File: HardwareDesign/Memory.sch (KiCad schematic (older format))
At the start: 4 parts, among them U200 28C256, U201 HM62256BLP-7SL

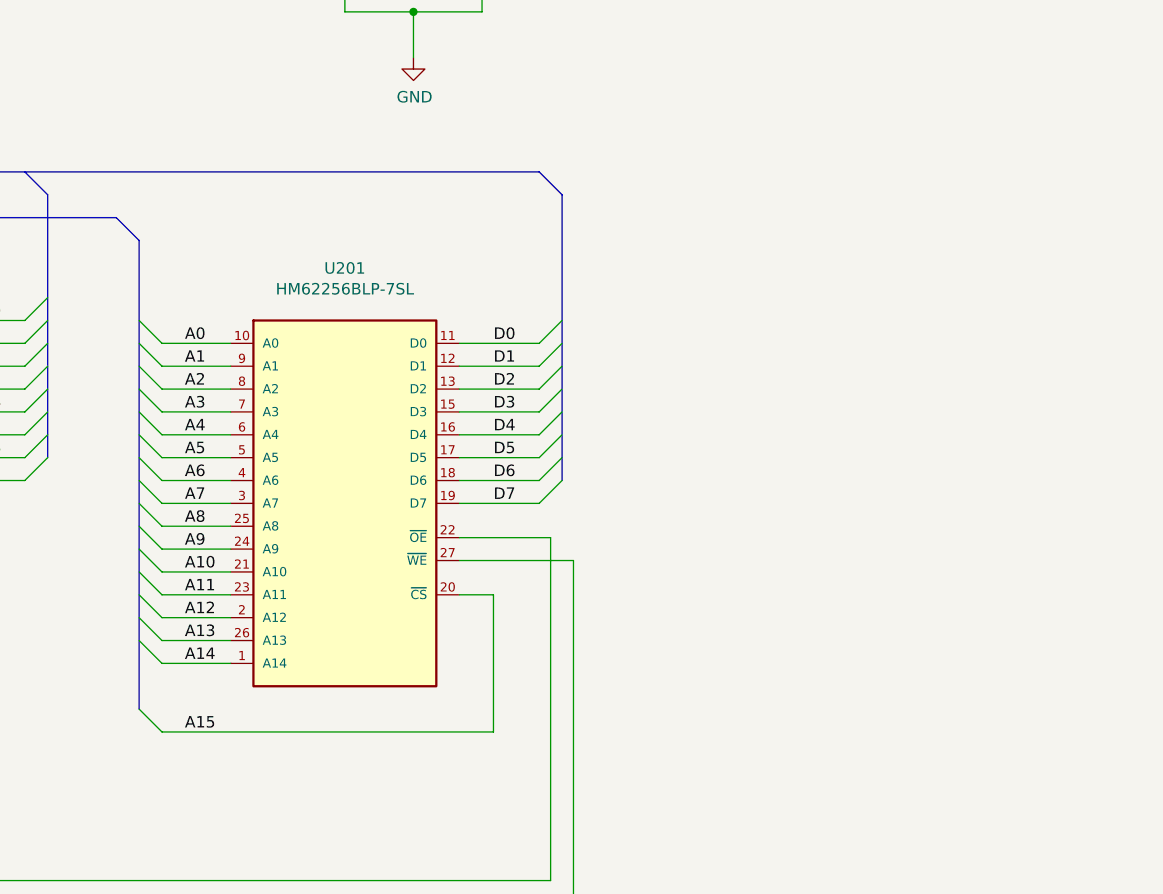
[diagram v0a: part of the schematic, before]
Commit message: added ~RAMEN~ backplane signals
Added a jumper so that the RAM chip can be configured
to use either A15 or ~RAMEN~ as its enable.

This change allows a CPU/glue logic module to have flexibility
regarding where the RAM is mapped.
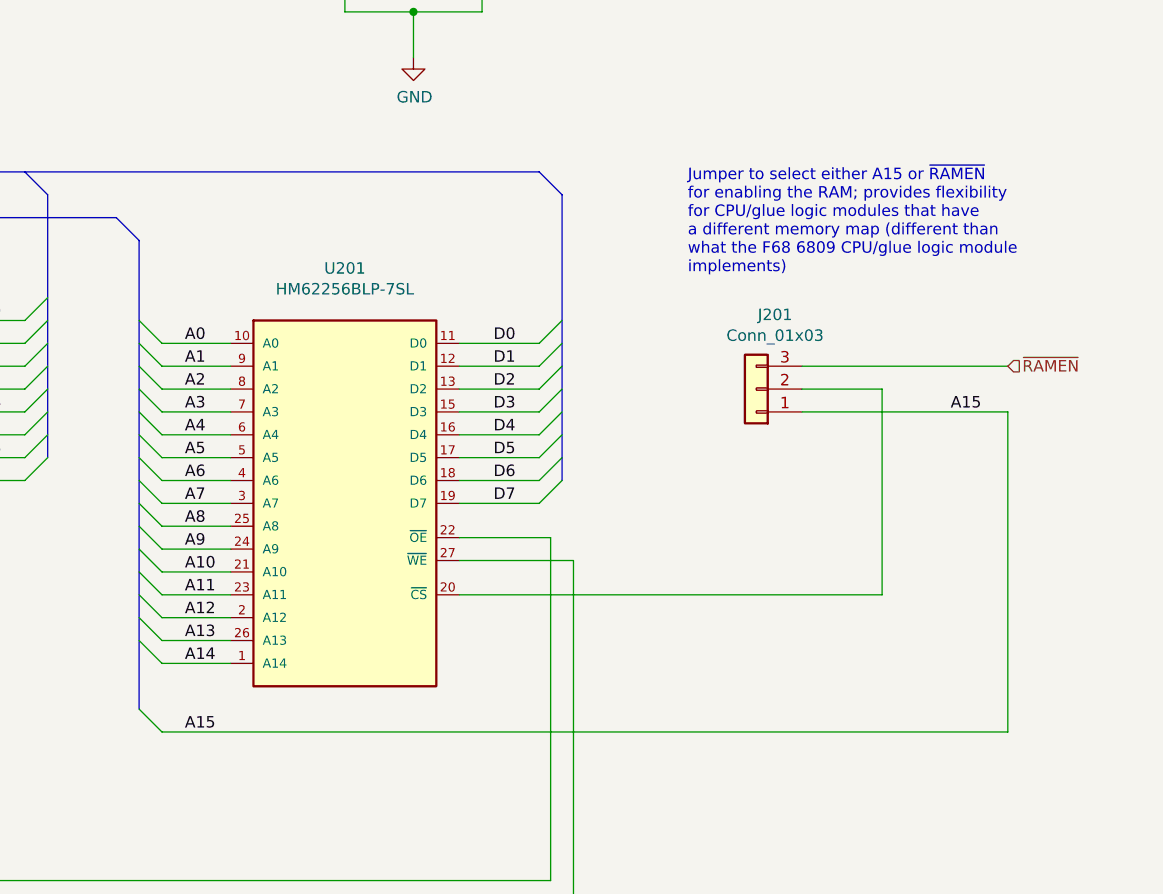
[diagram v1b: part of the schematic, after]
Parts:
- added J201: Conn_01x03, Connector_PinHeader_2.54mm:PinHeader_1x03_P2.54mm_Vertical, symbol Connector_Generic:Conn_01x03
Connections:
- net A15: now also J201.1 (Pin_1); no longer U201.20 (~CS)
- new net: J201.2 (Pin_2), U201.20 (~CS)
- new net ~RAMEN~: J201.3 (Pin_3)
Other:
- note added: "Jumper to select either A15 or ~RAMEN~\nfor enabling the RAM; provides flexibility\nfor CPU/glue logic modules that have\na different memory map (different than\nwhat the F68 6809 CPU/glue logic module\nimplements)"
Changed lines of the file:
@@
 Wire Wire Line
 	6600 6150 1050 6150
-Wire Wire Line
-	6250 5400 6250 4800
-Wire Wire Line
-	6250 4800 6100 4800
 Entry Wire Line
 	2050 3500 2150 3600
@@
 Entry Wire Line
 	1400 2700 1500 2800
-Wire Wire Line
-	6250 5400 4800 5400
-Entry Wire Line
-	4700 5300 4800 5400
+Text Notes 7100 3400 0    50   ~ 0
+Jumper to select either A15 or ~RAMEN~\nfor enabling the RAM; provides flexibility\nfor CPU/glue logic modules that have\na different memory map (different than\nwhat the F68 6809 CPU/glue logic module\nimplements)
+Wire Wire Line
+	7600 3800 8500 3800
+Wire Wire Line
+	7600 4000 8500 4000
 Text Label 4900 5400 0    50   ~ 0
 A15
+Text HLabel 8500 3800 2    50   Input ~ 0
+~RAMEN~
+$Comp
+L Connector_Generic:Conn_01x03 J201
+U 1 1 60D57AC9
+P 7400 3900
+F 0 "J201" H 7318 3575 50  0000 C CNN
+F 1 "Conn_01x03" H 7318 3666 50  0000 C CNN
+F 2 "Connector_PinHeader_2.54mm:PinHeader_1x03_P2.54mm_Vertical" H 7400 3900 50  0001 C CNN
+F 3 "~" H 7400 3900 50  0001 C CNN
+	1    7400 3900
+	-1   0    0    1
+$EndComp
+Entry Wire Line
+	4700 5300 4800 5400
+Wire Wire Line
+	4800 5400 8500 5400
+Wire Wire Line
+	8500 5400 8500 4000
+Text Label 8250 4000 0    50   ~ 0
+A15
+Wire Wire Line
+	6100 4800 7950 4800
+Wire Wire Line
+	7950 4800 7950 3900
+Wire Wire Line
+	7950 3900 7600 3900
 Wire Bus Line
 	3400 2950 6450 2950
@@
 	2050 3250 2050 4900
 Wire Bus Line
+	1500 1300 1500 3050
+Wire Bus Line
 	4700 3250 4700 5300
-Wire Bus Line
-	1500 1300 1500 3050
 $EndSCHEMATC
